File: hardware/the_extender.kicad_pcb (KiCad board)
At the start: 4 copper layers, 51.2 x 51.2 mm, 118 parts, among them J0 TYPE-C 24P QT 143, J1 TYPE-C-31-M-16, J2 U231-091N-3BLRC11, J3 PJ-327D-5A, J4 PJ-327D-5A, J5 AF 10.0 HC6.3, Q1 SSM3J332R,LF, U1 IP5306-I2C, U2 RP2040, U3 W25Q32JVSS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

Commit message: kinda did it
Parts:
- removed C20: 22u, Capacitor_SMD:C_1206_3216Metric_Pad1.33x1.80mm_HandSolder
- removed D3: LM3Z3V3T1G, Diode_SMD:D_SOD-323_HandSoldering
- removed R22: 4k7, Resistor_SMD:R_0805_2012Metric_Pad1.20x1.40mm_HandSolder
- removed R8, R9: 10k, Resistor_SMD:R_0805_2012Metric_Pad1.20x1.40mm_HandSolder
- added C47: 1u, Capacitor_SMD:C_0805_2012Metric_Pad1.18x1.45mm_HandSolder, F.Cu at (61.8, 38.7)
- added Q2: SSM3J332R,LF, Package_TO_SOT_SMD:SOT-23_Handsoldering, F.Cu at (55.9, 39.0)
- added Q3: SSM3J332R,LF, Package_TO_SOT_SMD:SOT-23_Handsoldering, F.Cu at (55.1, 24.8)
- added Q4: PMBT3904,215, Package_TO_SOT_SMD:SOT-23_Handsoldering, F.Cu at (59.9, 42.4)
- added R29: 10k, Resistor_SMD:R_0805_2012Metric_Pad1.20x1.40mm_HandSolder, F.Cu at (59.8, 38.6)
- C6: value 100n -> 22u; footprint Capacitor_SMD:C_0805_2012Metric_Pad1.18x1.45mm_HandSolder -> Capacitor_SMD:C_1206_3216Metric_Pad1.33x1.80mm_HandSolder
- J1: value TYPE-C-31-M-16 -> TYPE-C-31-M-16
- JP3: moved to F.Cu
- R1: value 5k1 -> 1k
- R2: value 5k1 -> 10k
- R3: value 4k7 -> 1k
- R4: value 4k7 -> 10k
- U1: value IP5306-I2C -> IP5310; footprint H3_Other:IP5306 -> easyeda2kicad:QFN-32_L5.0-W5.0-P0.50-BL-EP3.4
- moved R1 22.1 mm to (76.2, 30.0)
- moved R4 18.1 mm to (65.0, 42.4), turned to 0 degrees
- moved C6 16.3 mm to (48.6, 39.2)
- moved C19 14.4 mm to (59.8, 24.8), turned to -90 degrees
- moved R3 11.3 mm to (65.1, 34.0), turned to 0 degrees
- moved JP3 9.21 mm to (56.8, 35.6), turned to 0 degrees
- moved R2 7.75 mm to (61.8, 34.9), turned to -90 degrees
- moved D5 7.63 mm to (56.8, 35.6), turned to 180 degrees
- moved C17 5.64 mm to (59.6, 31.4), turned to -90 degrees
- moved C7 3.87 mm to (55.4, 30.2)
- moved R5 3.84 mm to (68.0, 32.0), turned to 180 degrees
- moved C12 3.80 mm to (55.4, 32.6)
- moved U1 1.75 mm to (63.9, 27.2), turned to 0 degrees
- moved C8 1.10 mm to (63.6, 31.7)
- moved C1 1.01 mm to (55.4, 27.8), turned to 0 degrees
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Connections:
- C12 pad 1: VBUS -> +5V
- C17 pad 1: VBUS -> +5V
- C19 pad 1: VBUS -> +5V
- C6 pad 1: CHG_VBUS -> VBUS
- C7 pad 1: VBUS -> +5V
- D1 pad 3: Net-(D1-BA) -> CHG_LED
- D5 pad 1: VBUS -> Net-(D5-K)
- JP3 pad 2: VBUS -> Net-(D5-K)
- L1 pad 1: Net-(U1-SW) -> Net-(L1-Pad1)
- R1 pad 1: GND -> Net-(U1-L2)
- R1 pad 2: CHG_CC2 -> +BATT
- R2 pad 1: GND -> Net-(Q3-G)
- R2 pad 2: CHG_CC1 -> +5V
- R3 pad 1: +3V3 -> Net-(U1-KEY)
- R3 pad 2: SCL -> REG5_KEY
- R4 pad 1: +3V3 -> Net-(Q4-B)
- R4 pad 2: SDA -> 5V_VBUS_EN
- U1 pad 1: CHG_VBUS -> Net-(U1-L2)
- U1 pad 2: SCL -> Net-(U1-L2)
- U1 pad 3: SDA -> unconnected-(U1-VSET-Pad3)
- U1 pad 4: PB_INT_RAW -> unconnected-(U1-VTHS-Pad4)
- U1 pad 5: Net-(U1-KEY) -> unconnected-(U1-RSET-Pad5)
- U1 pad 6: Net-(U1-BAT) -> unconnected-(U1-NTC-Pad6)
- U1 pad 7: Net-(U1-SW) -> GND
- U1 pad 8: +5V -> Net-(U1-KEY)
- U2 pad 17: CC_USB_INT -> 5V_VBUS_EN
- U2 pad 18: PB_INT -> CC_USB_INT
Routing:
- net Net-(Q3-G): track 0.00 -> 43.8 mm, vias 0 -> 3
- net PB_INT: track 36.0 -> 0.00 mm, vias 2 -> 0
- net VBUS: track 176.9 -> 144.8 mm, vias 18 -> 16
- net Net-(D1-BA): track 31.5 -> 0.00 mm
- net CHG_LED: track 0.00 -> 26.8 mm, vias 0 -> 2
- net 5V_VBUS_EN: track 0.00 -> 25.4 mm, vias 0 -> 3
- net CHG_VBUS: track 15.9 -> 36.1 mm, vias 0 -> 2
- net Net-(U1-L2): track 0.00 -> 19.8 mm, vias 0 -> 2
- net CHG_CC2: track 4.42 -> 22.3 mm, vias 0 -> 2
- net SDA: track 72.7 -> 56.0 mm, vias 4 -> 3
- net CHG_CC1: track 8.34 -> 24.2 mm, vias 0 -> 2
- net +5V: track 17.2 -> 31.4 mm, vias 4 -> 0
- net SCL: track 70.8 -> 57.5 mm, vias 4 -> 3
- net PB_INT_RAW: track 10.9 -> 0.00 mm
- net SND_LED_O: track 8.83 -> 0.00 mm
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- added copper zone on F.Cu, net +5V
- added copper zone on F.Cu, net Net-(L1-Pad1)
- added copper zone on F.Cu, net VBUS

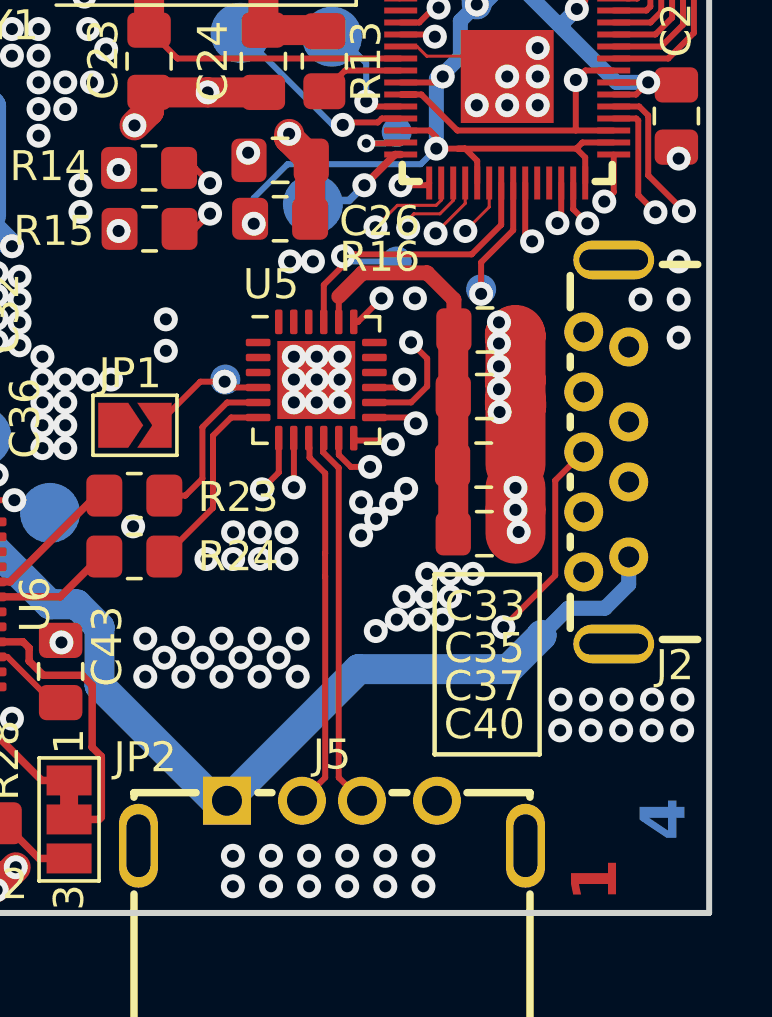
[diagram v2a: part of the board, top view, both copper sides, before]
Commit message: add way to measure VBUS
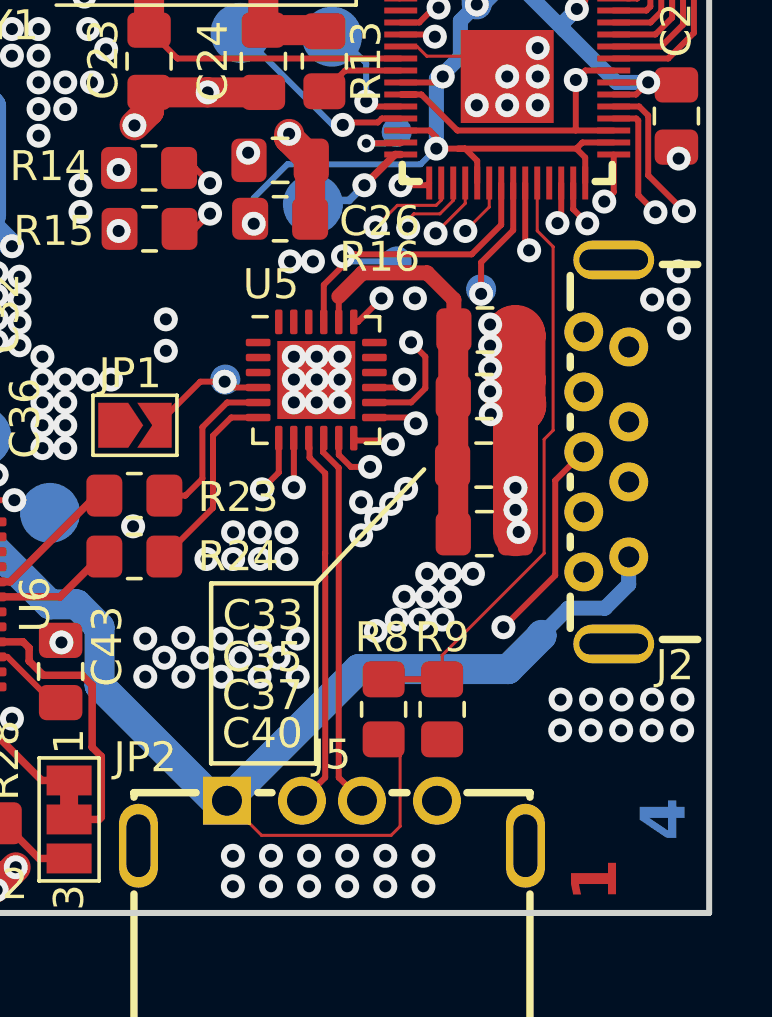
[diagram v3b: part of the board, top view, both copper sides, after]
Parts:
- added R8: 100k, Resistor_SMD:R_0805_2012Metric_Pad1.20x1.40mm_HandSolder, F.Cu at (86.0, 67.0)
- added R9: 100k, Resistor_SMD:R_0805_2012Metric_Pad1.20x1.40mm_HandSolder, F.Cu at (88.0, 67.0)
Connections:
- U2 pad 38: unconnected-(U2-GPIO26_ADC0-Pad38) -> RP_VBUS
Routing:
- net RP_VBUS: track 0.00 -> 20.2 mm
- net VBUS: track 144.8 -> 154.3 mm
- net GND: track 121.9 -> 122.7 mm

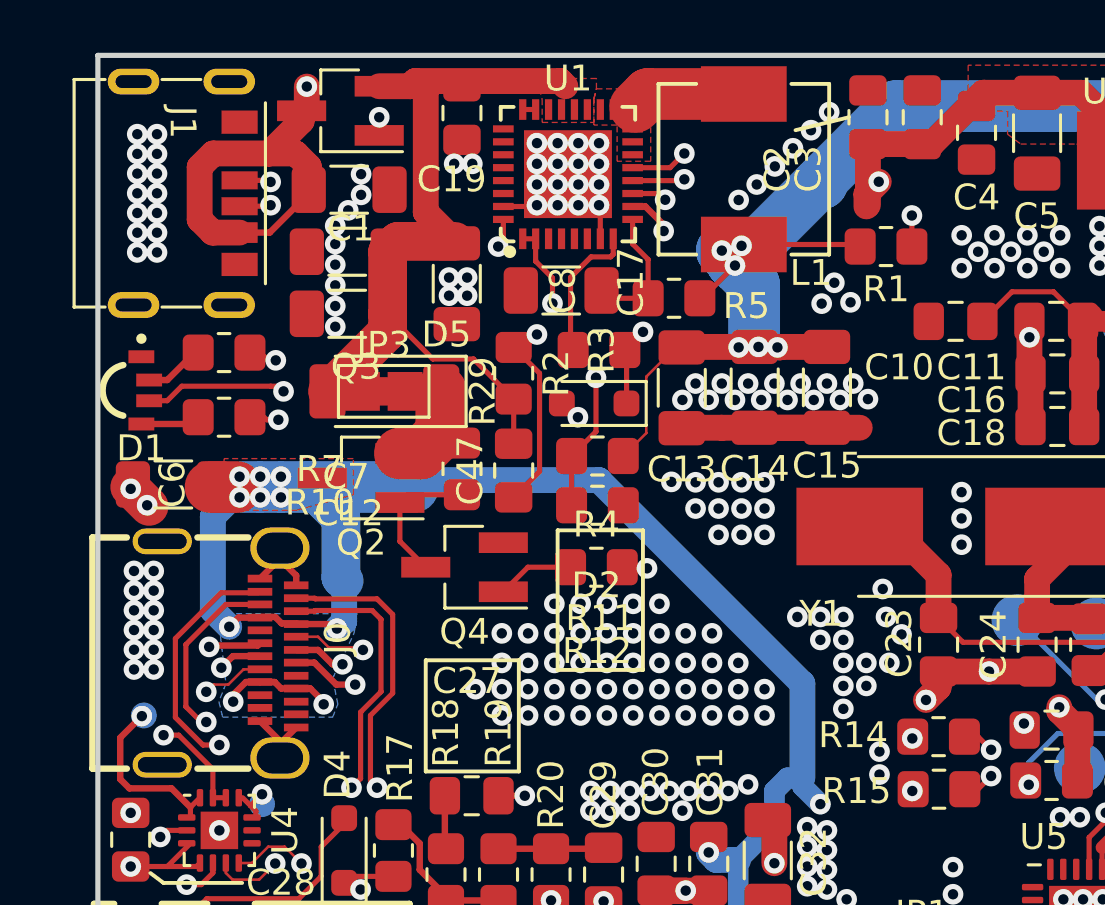
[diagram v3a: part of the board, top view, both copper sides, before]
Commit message: silk slightly less horrible
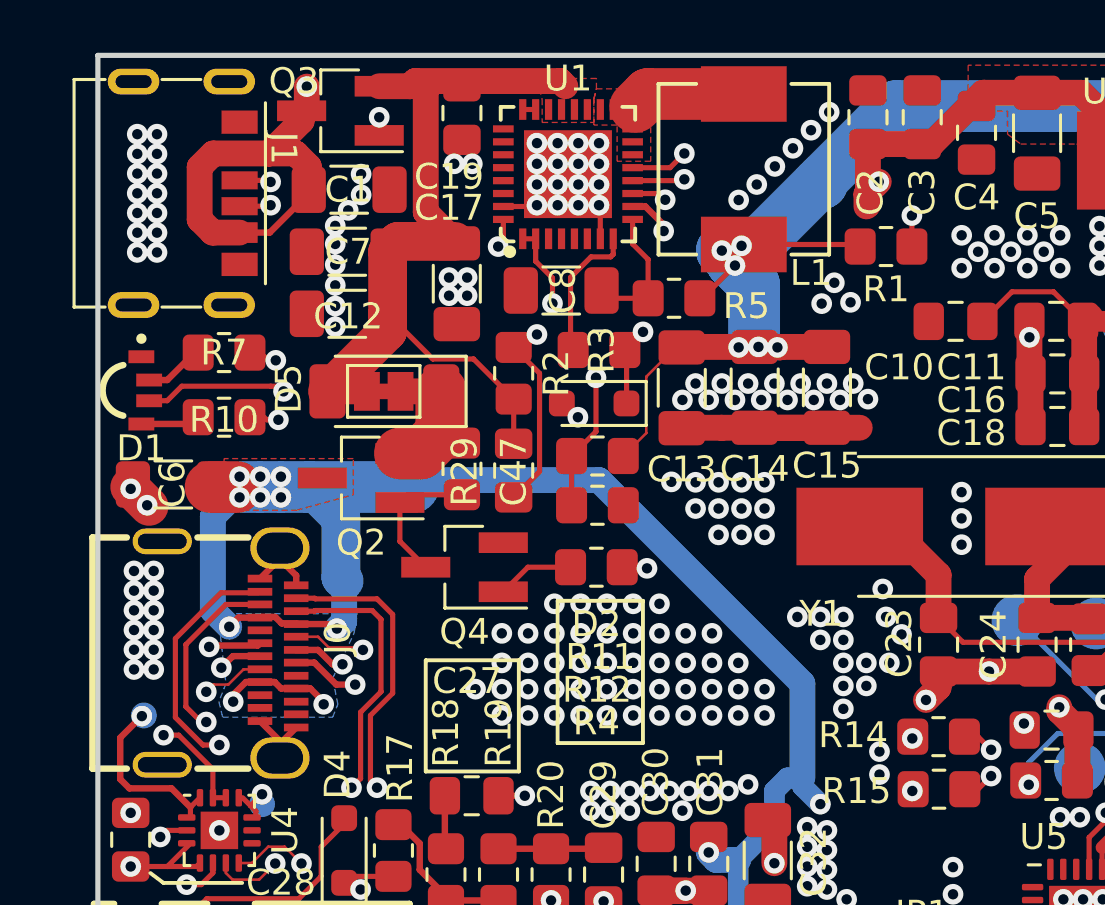
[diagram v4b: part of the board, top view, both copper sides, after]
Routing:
- net Net-(D5-K): track 6.10 -> 7.67 mm
- net +5V: track 31.4 -> 32.9 mm
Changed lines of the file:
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@@
     (property "ki_keywords" "cap capacitor")
     (attr smd)
-    (fp_text reference "C2" (at -2 -3.5 90) (layer "F.SilkS")
+    (fp_text reference "C2" (at -2.9 0.1 90) (layer "F.SilkS")
         (effects (font (size 1 1) (thickness 0.15)))
     )
@@
     (property "ki_keywords" "transistor PMOS P-MOS P-MOSFET")
     (attr smd)
-    (fp_text reference "Q3" (at -0.6 -9.9) (layer "F.SilkS")
+    (fp_text reference "Q3" (at 1.8 1.15) (layer "F.SilkS")
         (effects (font (size 1 1) (thickness 0.15)))
     )
@@
     (property "ki_keywords" "cap capacitor")
     (attr smd)
-    (fp_text reference "C17" (at -0.0625 -6.728 -270) (layer "F.SilkS")
+    (fp_text reference "C17" (at -2.9375 0.3 -180) (layer "F.SilkS")
         (effects (font (size 1 1) (thickness 0.15)))
     )
@@
     (property "ki_keywords" "cap capacitor")
     (attr smd)
-    (fp_text reference "C12" (at -0.0625 -7.714) (layer "F.SilkS")
+    (fp_text reference "C12" (at -0.0375 -0.1) (layer "F.SilkS")
         (effects (font (size 1 1) (thickness 0.15)))
     )
@@
     (property "ki_keywords" "cap capacitor")
     (attr smd)
-    (fp_text reference "C1" (at 0.0625 1.5) (layer "F.SilkS")
+    (fp_text reference "C1" (at -0.0375 0) (layer "F.SilkS")
         (effects (font (size 1 1) (thickness 0.15)))
     )
@@
     (property "ki_keywords" "cap capacitor")
     (attr smd)
-    (fp_text reference "C7" (at 0.047 -8.7) (layer "F.SilkS")
+    (fp_text reference "C7" (at -0.0375 0) (layer "F.SilkS")
         (effects (font (size 1 1) (thickness 0.15)))
     )
@@
     (property "ki_keywords" "diode Schottky")
     (attr smd exclude_from_bom)
-    (fp_text reference "D5" (at -2.4 2.2) (layer "F.SilkS")
+    (fp_text reference "D5" (at 3.7 0.1 90) (layer "F.SilkS")
         (effects (font (size 1 1) (thickness 0.15)))
     )
@@
     (property "ki_keywords" "cap capacitor")
     (attr smd)
-    (fp_text reference "C19" (at 2.5625 0.4 -180) (layer "F.SilkS")
+    (fp_text reference "C19" (at 2.4625 0.5 -180) (layer "F.SilkS")
         (effects (font (size 1 1) (thickness 0.15)))
     )
@@
     (property "ki_keywords" "cap capacitor")
     (attr smd)
-    (fp_text reference "C47" (at 0 -1.68 90) (layer "F.SilkS")
+    (fp_text reference "C47" (at -0.0375 0 90) (layer "F.SilkS")
         (effects (font (size 1 1) (thickness 0.15)))
     )
@@
     (property "ki_keywords" "cap capacitor")
     (attr smd)
-    (fp_text reference "C3" (at -2 -4.4 270) (layer "F.SilkS")
+    (fp_text reference "C3" (at -2.9 0 270) (layer "F.SilkS")
         (effects (font (size 1 1) (thickness 0.15)))
     )
@@
     (property "ki_keywords" "R res resistor")
     (attr smd)
-    (fp_text reference "R10" (at 3.7 3.3 180) (layer "F.SilkS")
+    (fp_text reference "R10" (at 0 0.1 180) (layer "F.SilkS")
         (effects (font (size 1 1) (thickness 0.15)))
     )
@@
     (property "ki_keywords" "R res resistor")
     (attr smd)
-    (fp_text reference "R11" (at -0.111 -6.27) (layer "F.SilkS")
+    (fp_text reference "R11" (at -0.111 -7.77) (layer "F.SilkS")
         (effects (font (size 1 1) (thickness 0.15)))
     )
@@
     (attr exclude_from_pos_files exclude_from_bom)
     (net_tie_pad_groups "1, 2")
-    (fp_text reference "JP3" (at 0 -1.8) (layer "F.SilkS")
+    (fp_text reference "JP3" (at 0 -1.8) (layer "F.SilkS") hide
         (effects (font (size 1 1) (thickness 0.15)))
     )
@@
     (fp_poly
       (pts
-        (xy -0.25 -0.55)
-        (xy 0.25 -0.55)
-        (xy 0.25 0.55)
-        (xy -0.25 0.55)
+        (xy -0.25 -0.3)
+        (xy 0.25 -0.3)
+        (xy 0.25 0.3)
+        (xy -0.25 0.3)
       )
       (stroke (width 0) (type solid)) (fill solid) (layer "F.Cu"))
-    (fp_line (start -1.75 -1) (end 1.75 -1)
+    (fp_line (start -1.4 -1) (end 1.4 -1)
       (stroke (width 0.12) (type solid)) (layer "F.SilkS"))
-    (fp_line (start -1.75 1) (end -1.75 -1)
+    (fp_line (start -1.4 1) (end -1.4 -1)
       (stroke (width 0.12) (type solid)) (layer "F.SilkS"))
-    (fp_line (start 1.75 -1) (end 1.75 1)
+    (fp_line (start 1.4 -1) (end 1.4 1)
       (stroke (width 0.12) (type solid)) (layer "F.SilkS"))
-    (fp_line (start 1.75 1) (end -1.75 1)
+    (fp_line (start 1.4 1) (end -1.4 1)
       (stroke (width 0.12) (type solid)) (layer "F.SilkS"))
-    (fp_line (start -2 -1.25) (end -2 1.25)
+    (fp_line (start -1.65 -1.25) (end -1.65 1.25)
       (stroke (width 0.05) (type solid)) (layer "F.CrtYd"))
-    (fp_line (start -2 -1.25) (end 2 -1.25)
+    (fp_line (start -1.65 -1.25) (end 1.65 -1.25)
       (stroke (width 0.05) (type solid)) (layer "F.CrtYd"))
-    (fp_line (start 2 1.25) (end -2 1.25)
+    (fp_line (start 1.65 1.25) (end -1.65 1.25)
       (stroke (width 0.05) (type solid)) (layer "F.CrtYd"))
-    (fp_line (start 2 1.25) (end 2 -1.25)
+    (fp_line (start 1.65 1.25) (end 1.65 -1.25)
       (stroke (width 0.05) (type solid)) (layer "F.CrtYd"))
-    (pad "1" smd rect (at -0.825 0) (size 1.35 1.5) (layers "F.Cu" "F.Mask")
+    (pad "1" smd rect (at -0.65 0) (size 1 1.5) (layers "F.Cu" "F.Mask")
       (net 1 "+5V") (pinfunction "A") (pintype "passive"))
-    (pad "2" smd rect (at 0.825 0) (size 1.35 1.5) (layers "F.Cu" "F.Mask")
+    (pad "2" smd rect (at 0.65 0) (size 1 1.5) (layers "F.Cu" "F.Mask")
       (net 136 "Net-(D5-K)") (pinfunction "B") (pintype "passive"))
   )
@@
     (property "ki_keywords" "R res resistor")
     (attr smd)
-    (fp_text reference "R4" (at 0 -1.65) (layer "F.SilkS")
+    (fp_text reference "R4" (at 0 6) (layer "F.SilkS")
         (effects (font (size 1 1) (thickness 0.15)))
     )
@@
     (property "ki_keywords" "R res resistor")
     (attr smd)
-    (fp_text reference "R29" (at -3 -0.8 90) (layer "F.SilkS")
+    (fp_text reference "R29" (at 0.1 -0.1 90) (layer "F.SilkS")
         (effects (font (size 1 1) (thickness 0.15)))
     )
@@
     (property "ki_keywords" "R res resistor")
     (attr smd)
-    (fp_text reference "R7" (at 3.7 4.5 180) (layer "F.SilkS")
+    (fp_text reference "R7" (at 0 0 180) (layer "F.SilkS")
         (effects (font (size 1 1) (thickness 0.15)))
     )
@@
     (property "ki_keywords" "diode")
     (attr smd)
-    (fp_text reference "D2" (at -0.087 -7.032 180) (layer "F.SilkS")
+    (fp_text reference "D2" (at -0.087 -8.532 180) (layer "F.SilkS")
         (effects (font (size 1 1) (thickness 0.15)))
     )
@@
     (property "ki_description" "USB 2.0-only Type-C Receptacle connector")
     (property "ki_keywords" "usb universal serial bus type-C USB2.0")
-    (fp_text reference "J1" (at -2.74 1.8 -90 unlocked) (layer "F.SilkS")
+    (fp_text reference "J1" (at -1.74 -2.1 -90 unlocked) (layer "F.SilkS")
         (effects (font (size 1 1) (thickness 0.15)))
     )
@@
     (property "ki_keywords" "R res resistor")
     (attr smd)
-    (fp_text reference "R12" (at -0.016 5.635) (layer "F.SilkS")
+    (fp_text reference "R12" (at -0.016 7.135) (layer "F.SilkS")
         (effects (font (size 1 1) (thickness 0.15)))
     )
@@
       (net 50 "Net-(U2-QSPI_SS)") (pinfunction "1") (pintype "passive"))
   )
-  (gr_rect (start 63.5 40.974) (end 66.8 46.374)
+  (gr_rect (start 63.5 43.7) (end 66.8 49.2)
     (stroke (width 0.15) (type default)) (fill none) (layer "F.SilkS"))
-  (gr_line (start 72.7 25.5) (end 74.765 25)
-    (stroke (width 0.15) (type default)) (layer "F.SilkS"))
   (gr_rect (start 80.3 62.8) (end 83.8 68.8)
     (stroke (width 0.15) (type default)) (fill none) (layer "F.SilkS"))
@@
   (segment (start 56.925 33.275) (end 54.6 35.6) (width 1.5) (layer "F.Cu") (net 1))
   (segment (start 56.925 32.6) (end 56.925 33.275) (width 1.5) (layer "F.Cu") (net 1))
+  (segment (start 56.125 35.6) (end 54.6 35.6) (width 1) (layer "F.Cu") (net 1))
   (segment (start 56.925 30.2) (end 57.325 29.8) (width 1.5) (layer "F.Cu") (net 1))
   (segment (start 58 23.6) (end 58.4 24) (width 1) (layer "F.Cu") (net 1))
@@
   (segment (start 59 35.6) (end 59 37.2) (width 2) (layer "F.Cu") (net 136))
   (segment (start 57.8 37.6) (end 57.4 38) (width 0.2) (layer "F.Cu") (net 136))
+  (segment (start 57.425 35.6) (end 59 35.6) (width 1) (layer "F.Cu") (net 136))
   (segment (start 59 37.2) (end 58.2 38) (width 2) (layer "F.Cu") (net 136))
   (segment (start 59.8 37.6) (end 57.8 37.6) (width 0.2) (layer "F.Cu") (net 136))
